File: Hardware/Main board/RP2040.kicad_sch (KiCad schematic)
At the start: 19 parts, among them U2 ABM8-272-T3, U4 RP2040

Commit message: Part selection
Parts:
- U2: JLCPCB Part # (none) -> C20625731; JLCPCB Parts URL (none) -> https://jlcpcb.com/partdetail/AbraconLlc-ABM8_272T3/C206257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; LCSC Part # (none) -> C20625731
- U4: JLCPCB Part # (none) -> C2040; JLCPCB Parts URL (none) -> https://jlcpcb.com/partdetail/RaspberryPi-RP2040/C2040; LCSC Part # (none) -> C2040
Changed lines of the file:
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@@
+			)
+		)
+		(property "JLCPCB Parts URL" "https://jlcpcb.com/partdetail/RaspberryPi-RP2040/C2040"
+			(at 106.68 110.49 0)
+			(effects
+				(font
+					(size 1.27 1.27)
+				)
+				(hide yes)
+			)
+		)
+		(property "JLCPCB Part #" "C2040"
+			(at 106.68 110.49 0)
+			(effects
+				(font
+					(size 1.27 1.27)
+				)
+				(hide yes)
+			)
+		)
+		(property "LCSC Part #" "C2040"
+			(at 106.68 110.49 0)
+			(effects
+				(font
+					(size 1.27 1.27)
+				)
+				(hide yes)
 			)
 		)
@@
 				(hide yes)
 			)
+		)
+		(property "JLCPCB Parts URL" "https://jlcpcb.com/partdetail/AbraconLlc-ABM8_272T3/C20625731"
+			(at 49.53 123.19 0)
+			(effects
+				(font
+					(size 1.27 1.27)
+				)
+				(hide yes)
+			)
+		)
+		(property "JLCPCB Part #" "C20625731"
+			(at 49.53 123.19 0)
+			(effects
+				(font
+					(size 1.27 1.27)
+				)
+				(hide yes)
+			)
+		)
+		(property "LCSC Part #" "C20625731"
+			(at 49.53 123.19 0)
+			(effects
+				(font
+					(size 1.27 1.27)
+				)
+				(hide yes)
+			)

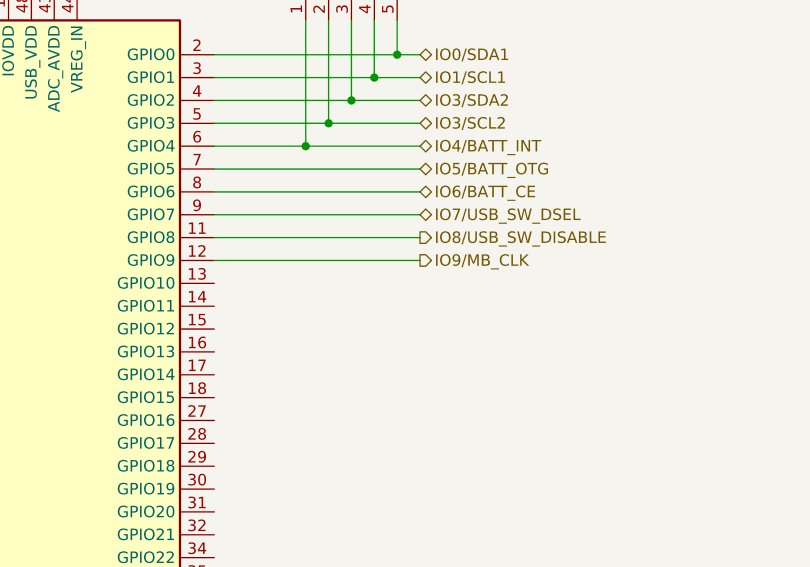
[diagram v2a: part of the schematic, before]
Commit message: Fixed BMS_STAT pin
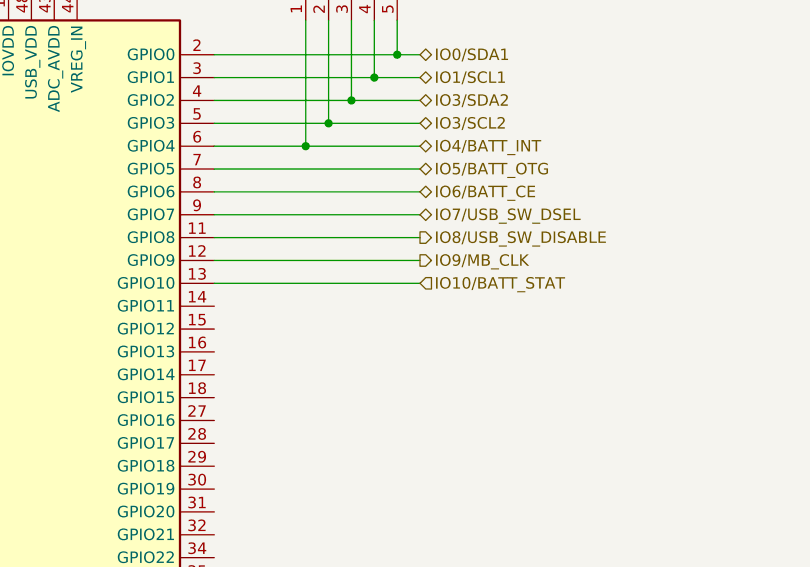
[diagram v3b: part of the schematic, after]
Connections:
- net IO10/BATT_STAT: now reaches U4.13 (GPIO10)
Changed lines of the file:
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@@
+	(wire
+		(pts
+			(xy 132.08 97.79) (xy 154.94 97.79)
+		)
+		(stroke
+			(width 0)
+			(type default)
+		)
+	)
 	(wire
 		(pts
@@
 		)
 	)
+	(hierarchical_label "IO10{slash}BATT_STAT"
+		(shape input)
+		(at 154.94 97.79 0)
+		(effects
+			(font
+				(size 1.27 1.27)
+			)
+			(justify left)
+		)
+	)

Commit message: Fix BMS_STAT pin
swapped RP2040 footprint for one with thermal vias
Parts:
- U4: footprint Package_DFN_QFN:QFN-56-1EP_7x7mm_P0.4mm_EP3.2x3.2mm -> Package_DFN_QFN:QFN-56-1EP_7x7mm_P0.4mm_EP3.2x3.2mm_ThermalVias
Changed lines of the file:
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@@
 			)
 		)
-		(property "Footprint" "Package_DFN_QFN:QFN-56-1EP_7x7mm_P0.4mm_EP3.2x3.2mm"
+		(property "Footprint" "Package_DFN_QFN:QFN-56-1EP_7x7mm_P0.4mm_EP3.2x3.2mm_ThermalVias"
 			(at 106.68 110.49 0)
 			(effects

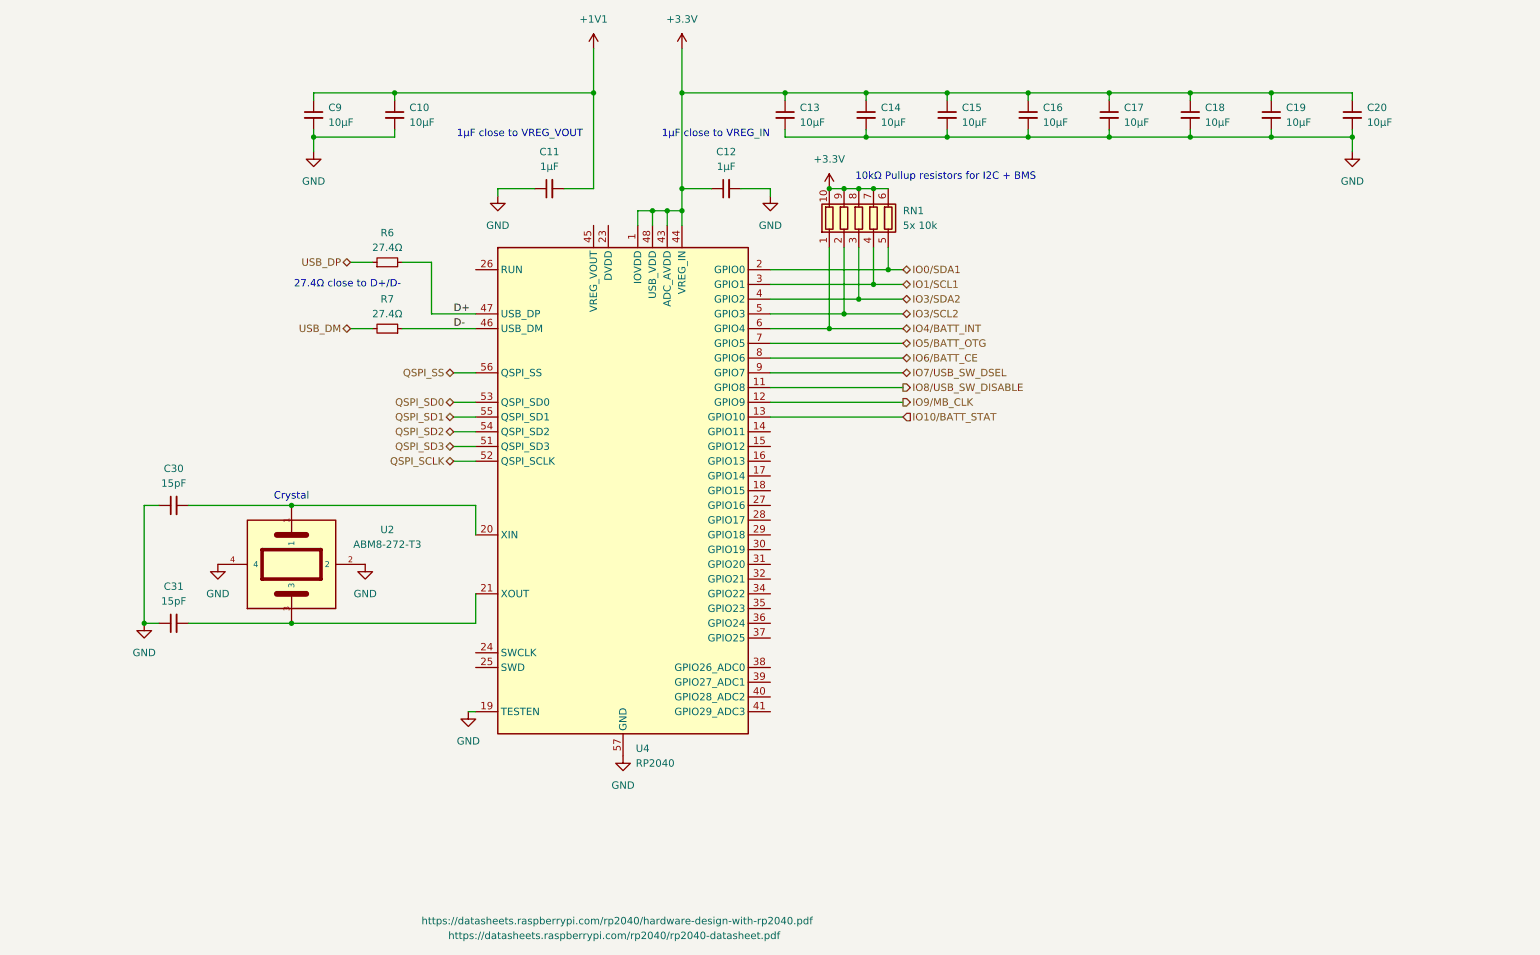
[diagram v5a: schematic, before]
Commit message: Update GND symbols
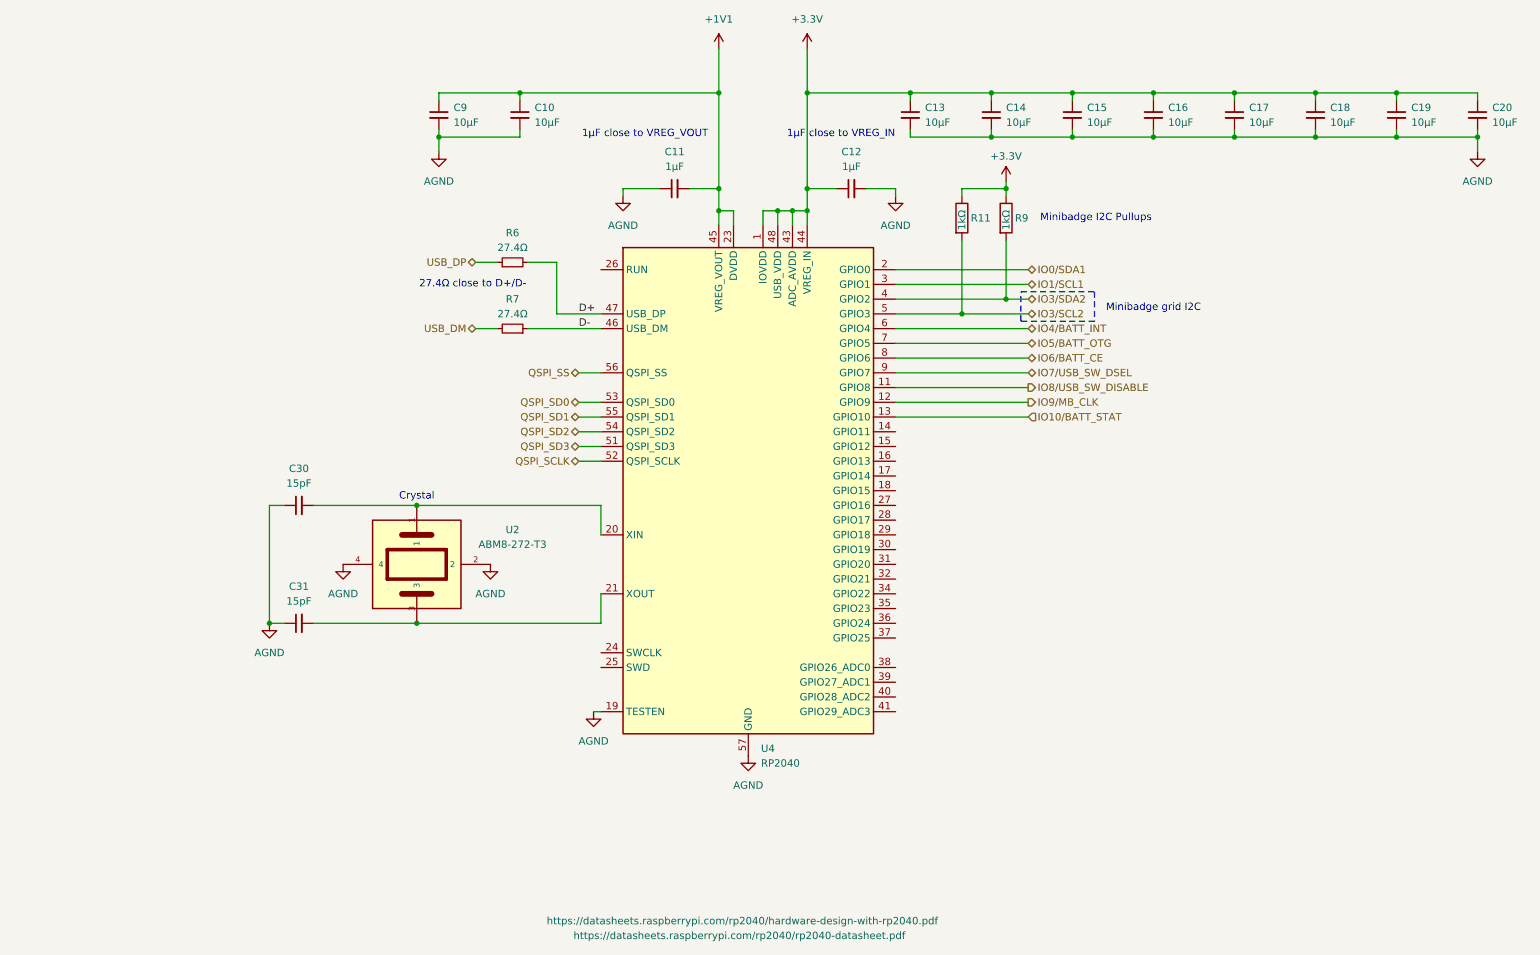
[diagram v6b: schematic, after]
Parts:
- removed RN1: 5x 10k, Resistor_SMD:R_Array_Convex_5x0603, symbol Device:R_Pack05
- added R11, R9: 1kΩ, symbol Device:R
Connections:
- net +1V1: now also U4.23 (DVDD), U4.45 (VREG_VOUT), U4.50 (DVDD)
- net +3.3V: now also R11.1, R9.1
- net IO3/SCL2: now also R11.2
- net IO3/SDA2: now also R9.2
- net GND renamed AGND
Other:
- note added: "Minibadge I2C Pullups"
- note added: "Minibadge grid I2C"
- note removed: "10kΩ Pullup resistors for I2C + BMS"
- moved on the sheet: C10, C11, C12, C13, C14, C15, C16, C17, C18, C19, C20, C30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

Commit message: refactor PCB for new BMS layout
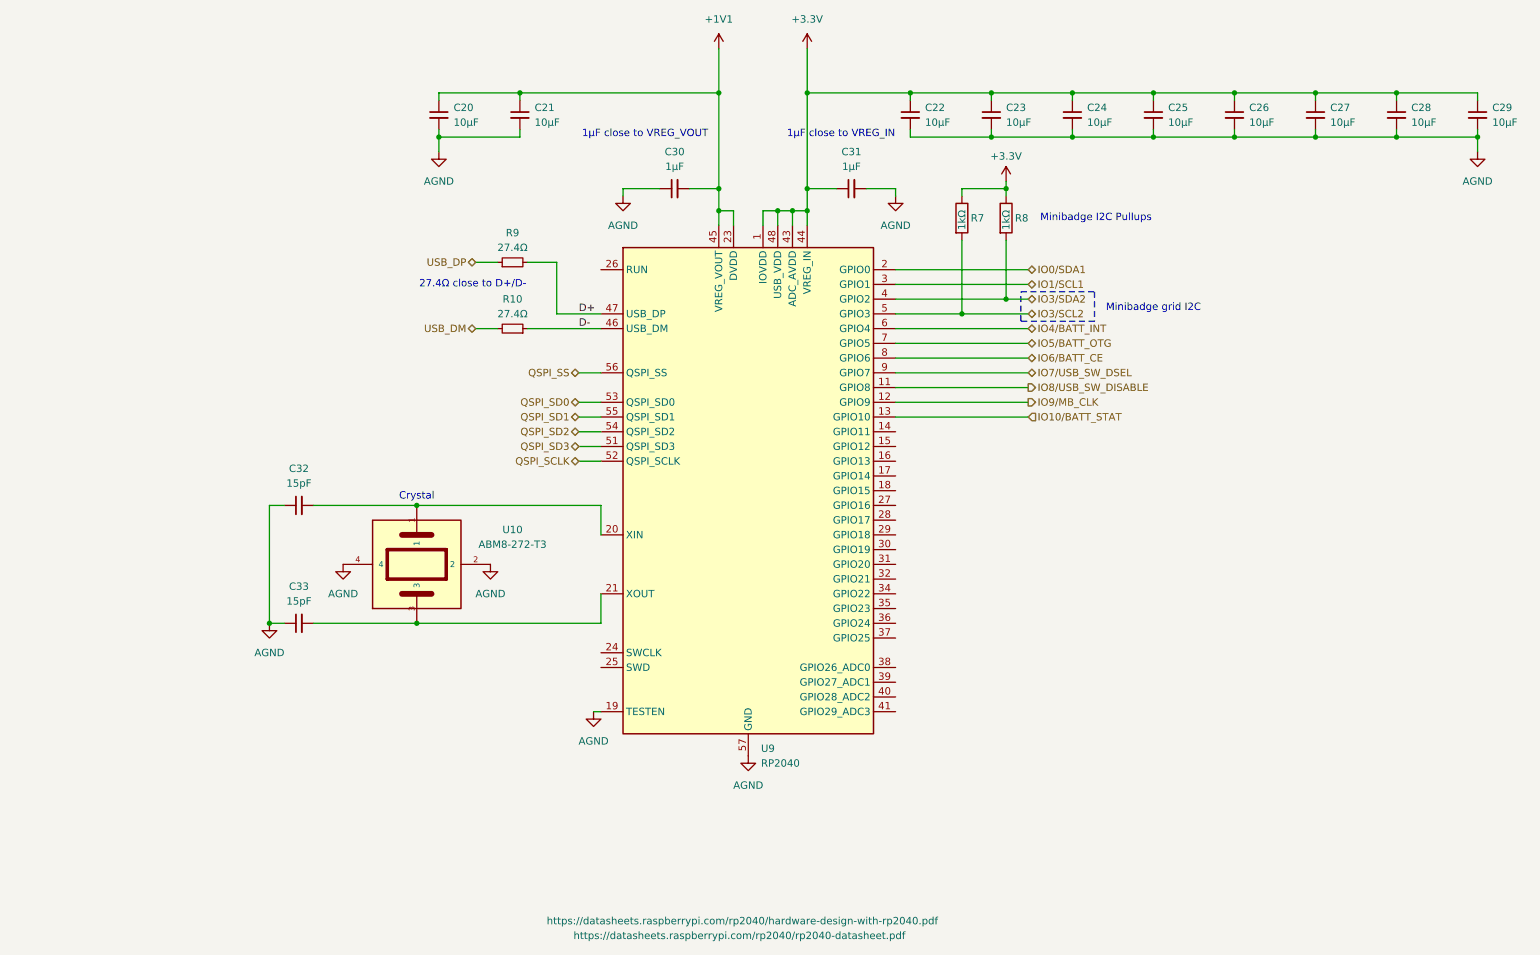
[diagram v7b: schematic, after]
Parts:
- R7: renamed from R11; footprint (none) -> Resistor_SMD:R_0603_1608Metric
- R8: renamed from R9; footprint (none) -> Resistor_SMD:R_0603_1608Metric
- renumbered C9 to C20, C10 to C21, C13 to C22, C14 to C23, C15 to C24, C16 to C25, C17 to C26, C18 to C27, C19 to C28, C20 to C29, C11 to C30, C12 to C31, C30 to C32, C31 to C33, R7 to R10, R6 to R9, U2 to U10, U4 to U9

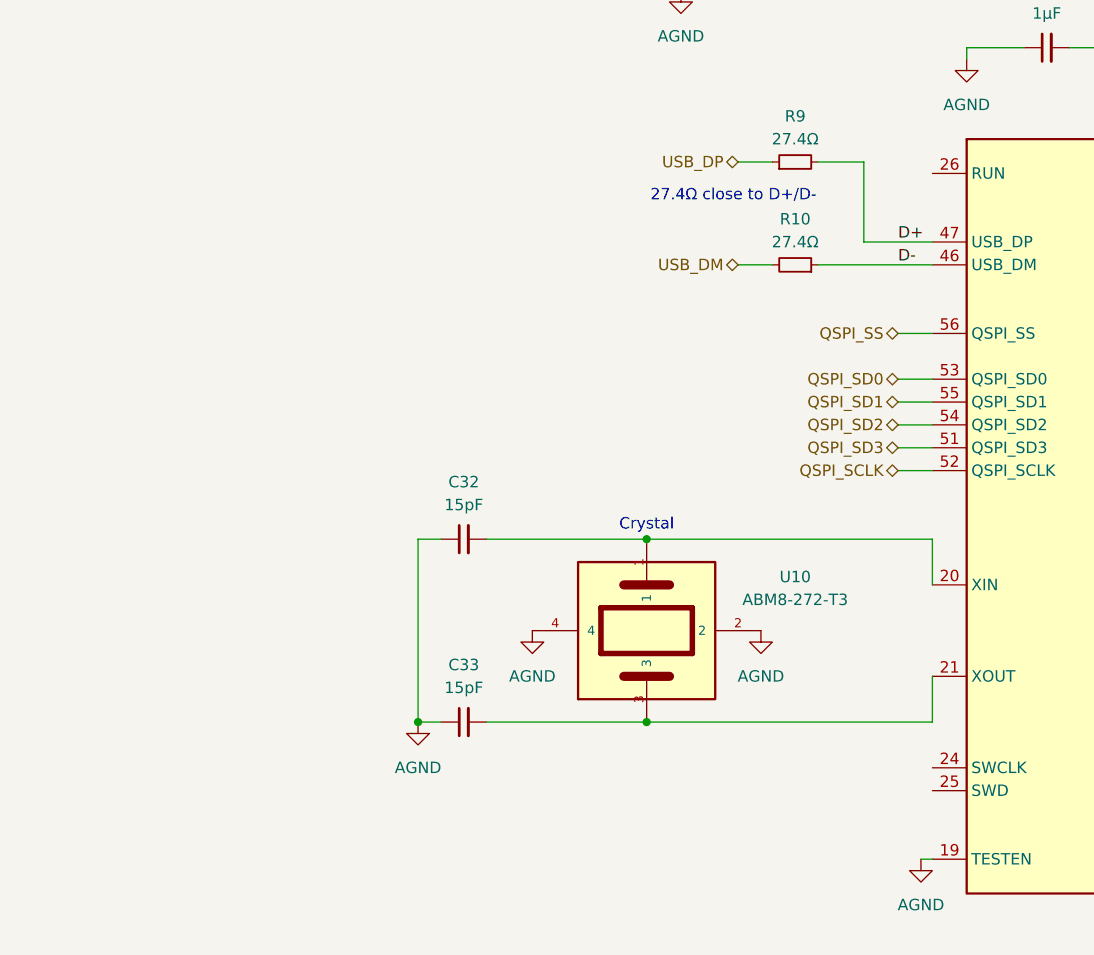
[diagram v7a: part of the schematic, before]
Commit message: debug pins for RP2040
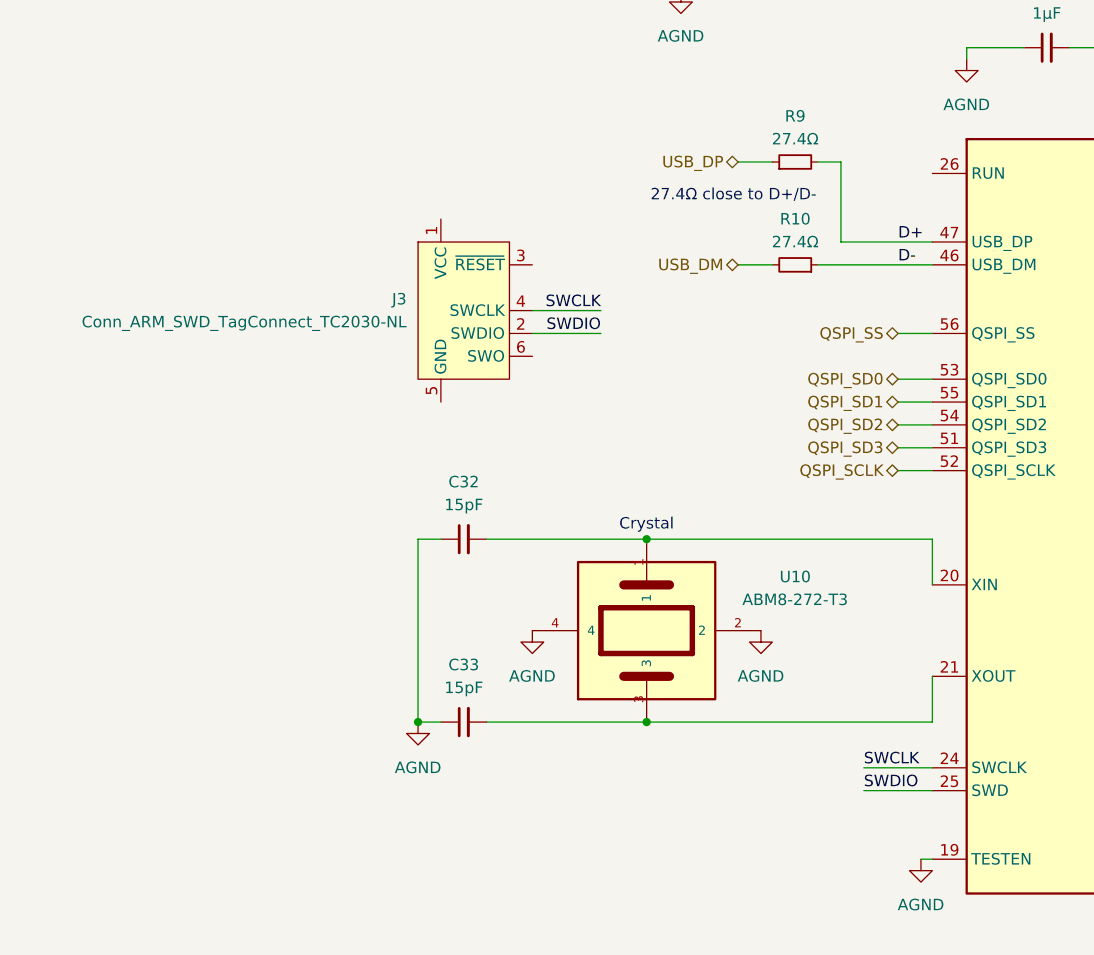
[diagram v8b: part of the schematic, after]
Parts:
- added J3: Conn_ARM_SWD_TagConnect_TC2030-NL, Connector:Tag-Connect_TC2030-IDC-NL_2x03_P1.27mm_Vertical, symbol Connector:Conn_ARM_SWD_TagConnect_TC2030-NL
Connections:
- net SWCLK: now reaches U9.24 (SWCLK)
- net SWCLK: now also J3.4 (SWCLK)
- net SWDIO: now reaches U9.25 (SWD)
- net SWDIO: now also J3.2 (SWDIO)
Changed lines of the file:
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@@
 	(wire
 		(pts
-			(xy 95.25 80.01) (xy 102.87 80.01)
+			(xy 92.71 80.01) (xy 102.87 80.01)
 		)
 		(stroke
@@
 	(wire
 		(pts
+			(xy 66.04 90.17) (xy 58.42 90.17)
+		)
+		(stroke
+			(width 0)
+			(type default)
+		)
+	)
+	(wire
+		(pts
 			(xy 138.43 58.42) (xy 138.43 62.23)
 		)
@@
 	(wire
 		(pts
+			(xy 95.25 138.43) (xy 102.87 138.43)
+		)
+		(stroke
+			(width 0)
+			(type default)
+		)
+	)
+	(wire
+		(pts
 			(xy 99.06 95.25) (xy 102.87 95.25)
 		)
@@
 	(wire
 		(pts
-			(xy 95.25 71.12) (xy 95.25 80.01)
+			(xy 92.71 71.12) (xy 92.71 80.01)
 		)
 		(stroke
@@
 	(wire
 		(pts
+			(xy 66.04 87.63) (xy 58.42 87.63)
+		)
+		(stroke
+			(width 0)
+			(type default)
+		)
+	)
+	(wire
+		(pts
 			(xy 99.06 102.87) (xy 102.87 102.87)
 		)
@@
 	(wire
 		(pts
-			(xy 90.17 71.12) (xy 95.25 71.12)
+			(xy 90.17 71.12) (xy 92.71 71.12)
 		)
 		(stroke
@@
 		(pts
 			(xy 90.17 82.55) (xy 102.87 82.55)
+		)
+		(stroke
+			(width 0)
+			(type default)
+		)
+	)
+	(wire
+		(pts
+			(xy 95.25 140.97) (xy 102.87 140.97)
 		)
 		(stroke
@@
 		)
 	)
+	(label "SWCLK"
+		(at 66.04 87.63 180)
+		(effects
+			(font
+				(size 1.27 1.27)
+			)
+			(justify right bottom)
+		)
+	)
+	(label "SWCLK"
+		(at 95.25 138.43 0)
+		(effects
+			(font
+				(size 1.27 1.27)
+			)
+			(justify left bottom)
+		)
+	)
+	(label "SWDIO"
+		(at 66.04 90.17 180)
+		(effects
+			(font
+				(size 1.27 1.27)
+			)
+			(justify right bottom)
+		)
+	)
 	(label "D+"
 		(at 99.06 80.01 0)
+		(effects
+			(font
+				(size 1.27 1.27)
+			)
+			(justify left bottom)
+		)
+	)
+	(label "SWDIO"
+		(at 95.25 140.97 0)
 		(effects
 			(font
@@
 					(unit 1)
 				)
+			)
+		)
+	)
+	(symbol
+		(lib_id "Connector:Conn_ARM_SWD_TagConnect_TC2030-NL")
+		(at 50.8 87.63 0)
+		(unit 1)
+		(exclude_from_sim no)
+		(in_bom no)
+		(on_board yes)
+		(dnp no)
+		(fields_autoplaced yes)
+		(property "Reference" "J3"
+			(at 44.45 86.3599 0)
+			(effects
+				(font
+					(size 1.27 1.27)
+				)
+				(justify right)
+			)
+		)
+		(property "Value" "Conn_ARM_SWD_TagConnect_TC2030-NL"
+			(at 44.45 88.8999 0)
+			(effects
+				(font
+					(size 1.27 1.27)
+				)
+				(justify right)
+			)
+		)
+		(property "Footprint" "Connector:Tag-Connect_TC2030-IDC-NL_2x03_P1.27mm_Vertical"
+			(at 50.8 105.41 0)
+			(effects
+				(font
+					(size 1.27 1.27)
+				)
+				(hide yes)
+			)
+		)
+		(property "Datasheet" "https://www.tag-connect.com/wp-content/uploads/bsk-pdf-manager/TC2030-CTX_1.pdf"
+			(at 50.8 102.87 0)
+			(effects
+				(font
+					(size 1.27 1.27)
+				)
+				(hide yes)
+			)
+		)
+		(property "Description" "Tag-Connect ARM Cortex SWD JTAG connector, 6 pin, no legs"
+			(at 50.8 87.63 0)
+			(effects
+				(font
+					(size 1.27 1.27)
+				)
+				(hide yes)
+			)
+		)
+		(pin "5"
+		)
+		(pin "6"
+		)
+		(pin "4"
+		)
+		(pin "3"
+		)
+		(pin "1"
+		)
+		(pin "2"
+		)
+		(instances
+			(project ""
+				(path "/e5119d15-74fb-4259-abbc-5cab1f368532/9c03ac80-c552-4a59-83c4-4e8b67a63031"
+					(reference "J3")
+					(unit 1)
+				)
